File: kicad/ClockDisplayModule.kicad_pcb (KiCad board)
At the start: 2 copper layers, 88.9 x 33 mm, 13 parts, among them P101 CONN_01X05, U101 MAX7221

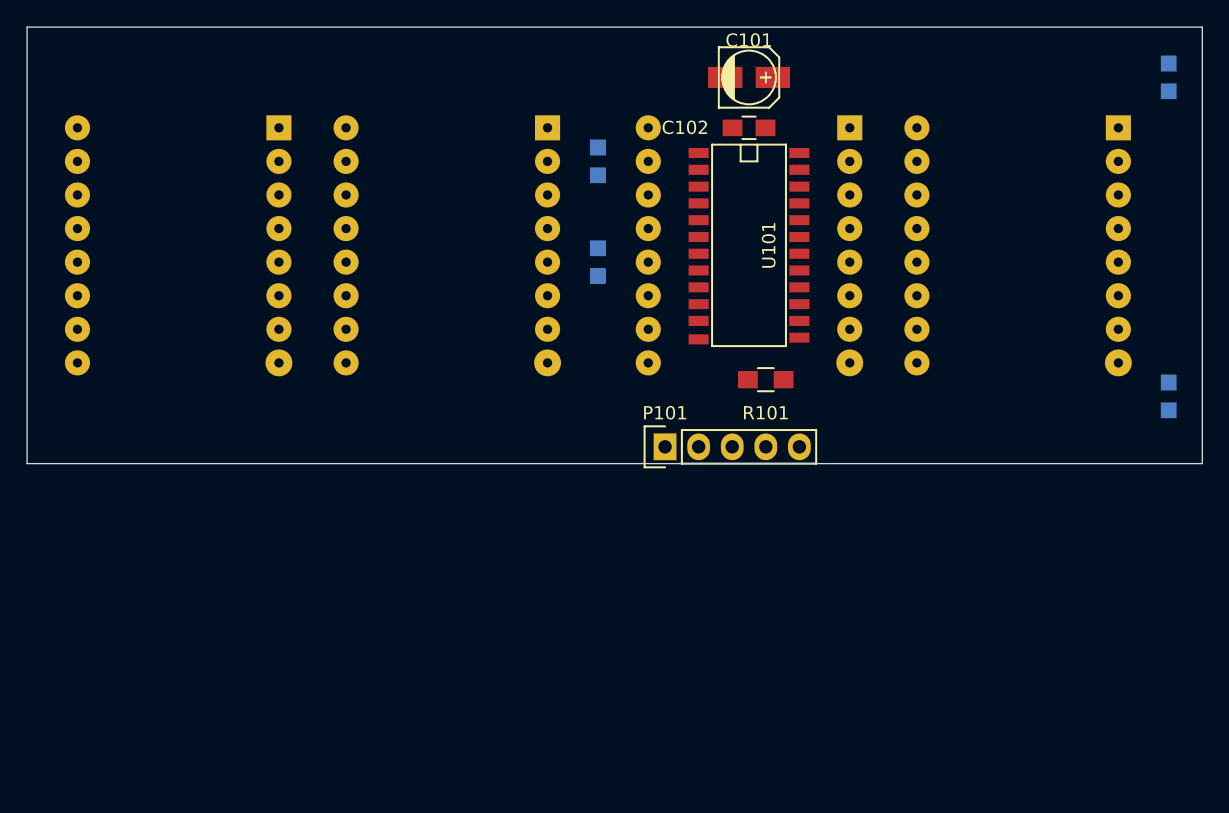
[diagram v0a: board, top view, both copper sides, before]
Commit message: Initial trail of the layout. The given board is not big enough
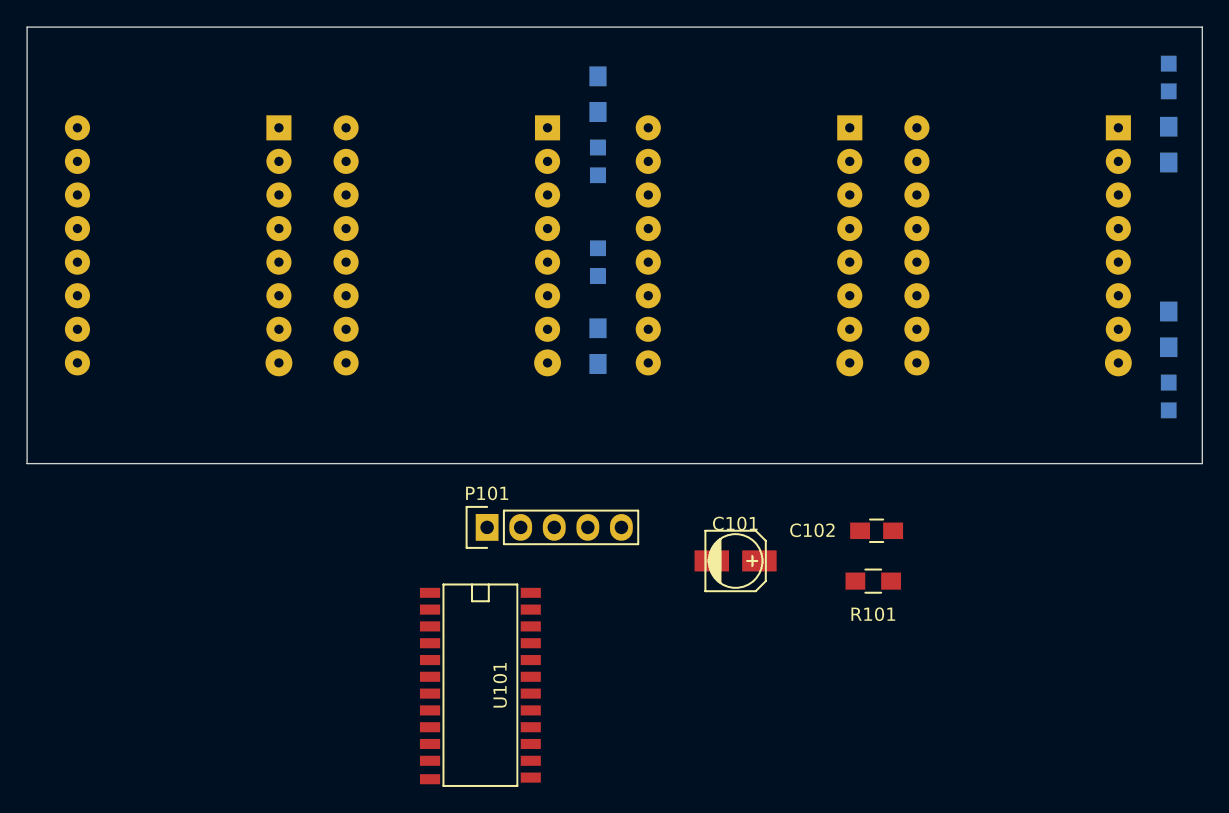
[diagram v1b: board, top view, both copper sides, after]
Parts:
- added R102: 0, Resistors_SMD:R_0805_HandSoldering, B.Cu at (114.3, 40.6)
- added R103: 0, Resistors_SMD:R_0805_HandSoldering, B.Cu at (114.3, 59.7)
- added R104: 0, Resistors_SMD:R_0805_HandSoldering, B.Cu at (157.5, 58.4)
- added R105: 0, Resistors_SMD:R_0805_HandSoldering, B.Cu at (157.5, 44.5)
- AFF101, AFF102, AFF103, AFF104: value 7SEGMENTS-CC -> SC08-11SURKWA
- moved U101 39.0 mm to (105.4, 85.3)
- moved C101 36.6 mm to (124.7, 75.9)
- moved C102 32.0 mm to (135.4, 73.7)
- moved R101 17.3 mm to (135.1, 77.5)
- moved P101 14.8 mm to (105.9, 73.4)
- turned D102 to 270 degrees
- turned D104 to 270 degrees
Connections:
- AFF101 pad 1: Seg_E -> Seg_A
- AFF101 pad 10: Seg_G -> Seg_D
- AFF101 pad 11: (no net) -> Dig_0
- AFF101 pad 12: (no net) -> Seg_C
- AFF101 pad 13: (no net) -> Seg_G
- AFF101 pad 14: (no net) -> Seg_B
- AFF101 pad 16: (no net) -> Dig_0
- AFF101 pad 2: Seg_D -> Seg_F
- AFF101 pad 4: Seg_C -> Seg_E
- AFF101 pad 5: Net-(AFF101-Pad5) -> Dig_0
- AFF101 pad 6: Seg_B -> (no net)
- AFF101 pad 7: Seg_A -> (no net)
- AFF101 pad 8: Dig_0 -> (no net)
- AFF101 pad 9: Seg_F -> (no net)
- AFF102 pad 1: Seg_E -> Seg_A
- AFF102 pad 10: Seg_G -> Seg_D
- AFF102 pad 11: (no net) -> Dig_1
- AFF102 pad 12: (no net) -> Seg_C
- AFF102 pad 13: (no net) -> Seg_G
- AFF102 pad 14: (no net) -> Seg_B
- AFF102 pad 16: (no net) -> Dig_1
- AFF102 pad 2: Seg_D -> Seg_F
- AFF102 pad 4: Seg_C -> Seg_E
- AFF102 pad 5: Net-(AFF102-Pad5) -> Dig_1
- AFF102 pad 6: Seg_B -> (no net)
- AFF102 pad 7: Seg_A -> (no net)
- AFF102 pad 8: Dig_1 -> (no net)
- AFF102 pad 9: Seg_F -> (no net)
- AFF103 pad 1: Seg_E -> Seg_A
- AFF103 pad 10: Seg_G -> Seg_D
- AFF103 pad 11: (no net) -> Dig_2
- AFF103 pad 12: (no net) -> Seg_C
- AFF103 pad 13: (no net) -> Seg_G
- AFF103 pad 14: (no net) -> Seg_B
- AFF103 pad 16: (no net) -> Dig_2
- AFF103 pad 2: Seg_D -> Seg_F
- AFF103 pad 4: Seg_C -> Seg_E
- AFF103 pad 5: Net-(AFF103-Pad5) -> Dig_2
- AFF103 pad 6: Seg_B -> (no net)
- AFF103 pad 7: Seg_A -> (no net)
- AFF103 pad 8: Dig_2 -> (no net)
- AFF103 pad 9: Seg_F -> (no net)
- AFF104 pad 1: Seg_E -> Seg_A
- AFF104 pad 10: Seg_G -> Seg_D
- AFF104 pad 11: (no net) -> Dig_3
- AFF104 pad 12: (no net) -> Seg_C
- AFF104 pad 13: (no net) -> Seg_G
- AFF104 pad 14: (no net) -> Seg_B
- AFF104 pad 16: (no net) -> Dig_3
- AFF104 pad 2: Seg_D -> Seg_F
- AFF104 pad 4: Seg_C -> Seg_E
- AFF104 pad 5: Net-(AFF104-Pad5) -> Dig_3
- AFF104 pad 6: Seg_B -> (no net)
- AFF104 pad 7: Seg_A -> (no net)
- AFF104 pad 8: Dig_3 -> (no net)
- AFF104 pad 9: Seg_F -> (no net)
- D101 pad 2: Seg_A -> Net-(D101-Pad2)
- D102 pad 2: Seg_B -> Net-(D102-Pad2)
- D103 pad 2: Seg_C -> Net-(D103-Pad2)
- D104 pad 2: Seg_D -> Net-(D104-Pad2)
- U101 pad 10: Net-(U101-Pad10) -> Signal
- U101 pad 22: Net-(U101-Pad22) -> (no net)
- U101 pad 24: Net-(U101-Pad24) -> (no net)
- U101 pad 3: Signal -> (no net)
- U101 pad 5: Net-(U101-Pad5) -> (no net)
- U101 pad 8: Net-(U101-Pad8) -> (no net)
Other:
- net class Default: clearance 0.2 -> 0.1524; trace_width 0.25 -> 0.1524; via_dia 0.6 -> 0.6858; via_drill 0.4 -> 0.3302
- rule trace_clearance: 0.2 -> 0.1524
- rule trace_min: 0.2 -> 0.1524
- rule via_min_drill: 0.3 -> 0.3302
- rule via_min_size: 0.4 -> 0.6858
